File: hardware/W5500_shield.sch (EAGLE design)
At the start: 30 parts, among them IC1 WIZ5500, IC2 741G07S0T23-5-HAND, X1 MEGA2560, Y1 25MHz

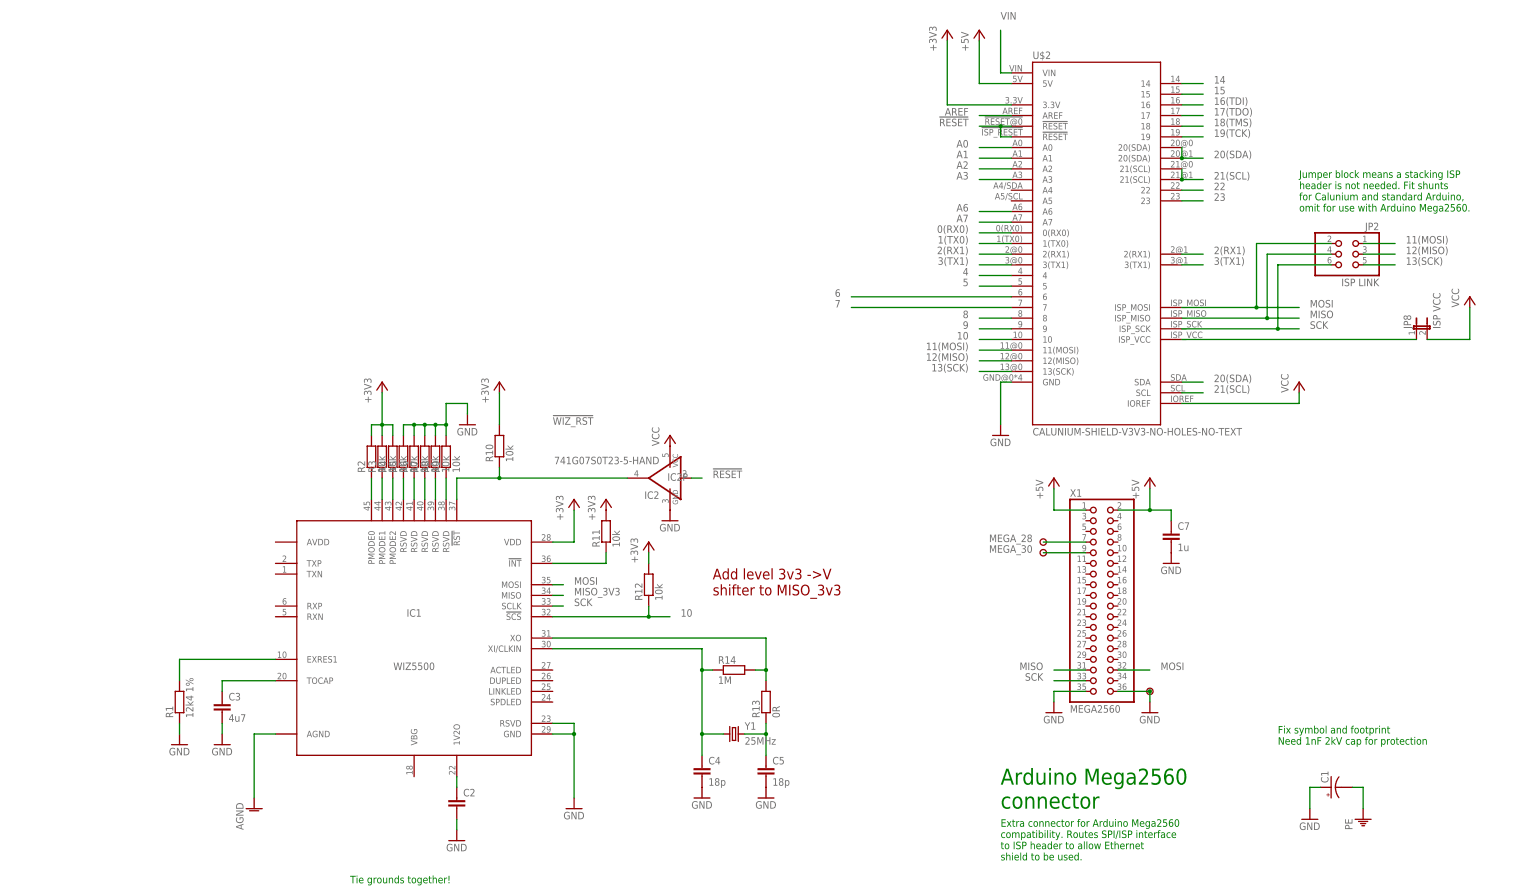
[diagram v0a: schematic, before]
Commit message: Update W5500 shield
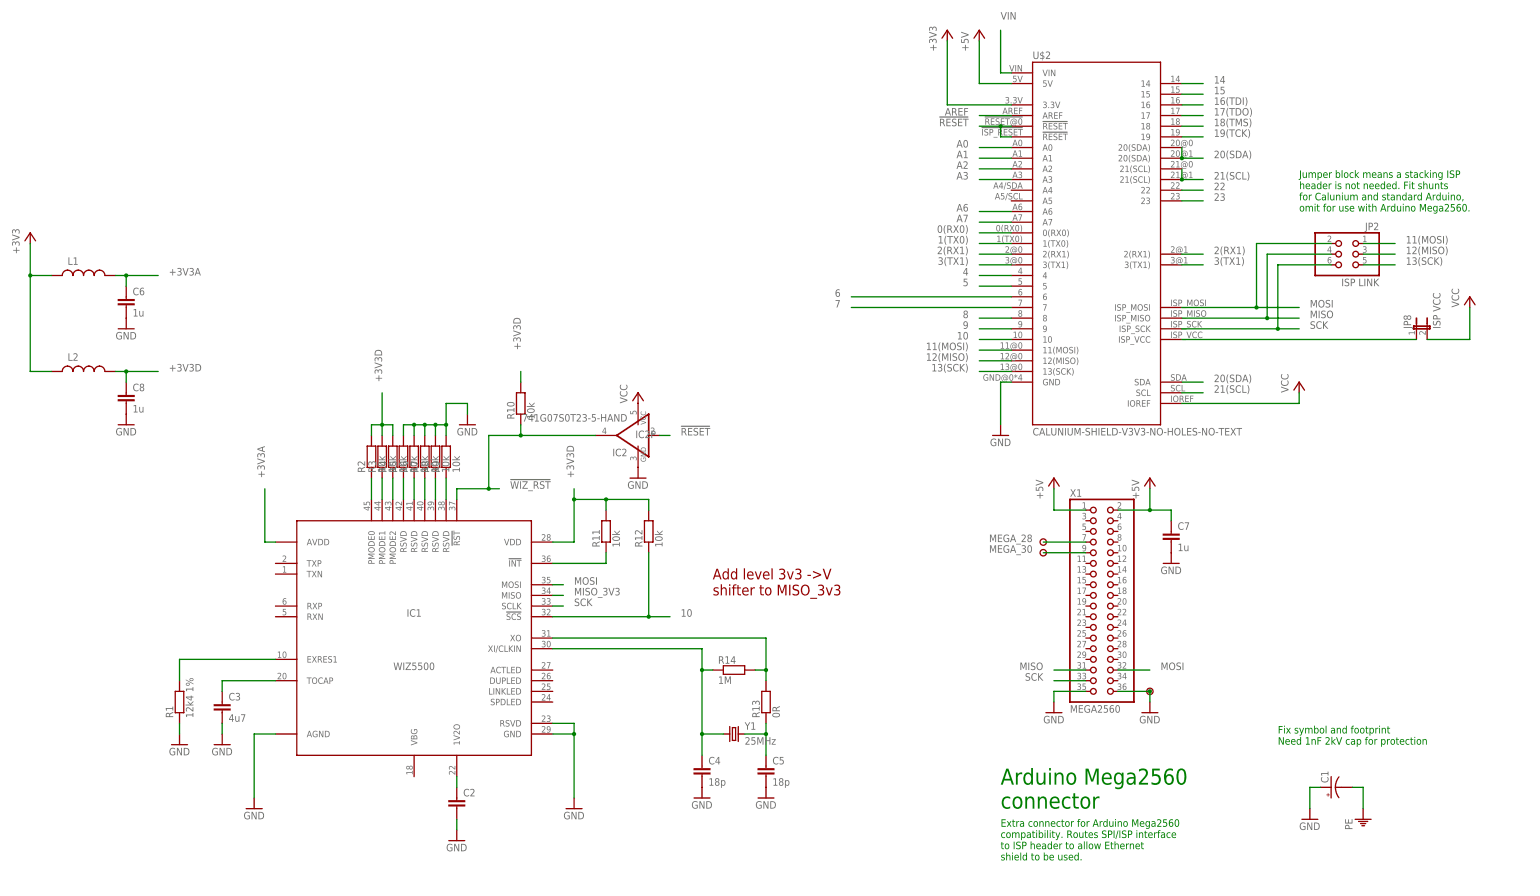
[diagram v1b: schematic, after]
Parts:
- added C6, C8: 1u, SteveMarple:C-EU1206-HAND
- added L1, L2: (no value), SteveMarple:INDUCTOR0805-HAND
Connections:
- removed net AGND: IC1.AGND
- new net +3V3A: C6.1, IC1.AVDD, L1.2
- new net +3V3D: C8.1, IC1.VDD, L2.2, R10.2, R11.2, R12.2, R2.2, R3.2, R4.2
- net +3V3: now also L1.1, L2.1; no longer IC1.VDD, R10.2, R11.2, R12.2, R2.2, R3.2, R4.2
- net GND: now also C6.2, C8.2, IC1.AGND
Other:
- note removed: "Tie grounds together!"
- moved on the sheet: IC2, IC2P, R10, R12
